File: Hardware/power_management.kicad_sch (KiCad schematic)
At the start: 37 parts, among them J2 Conn_01x03, SW27 SW_DPDT_x2, U2 BQ24040, U3 BQ51050BRHL, U4 AP22814BW5, U5 AP7333

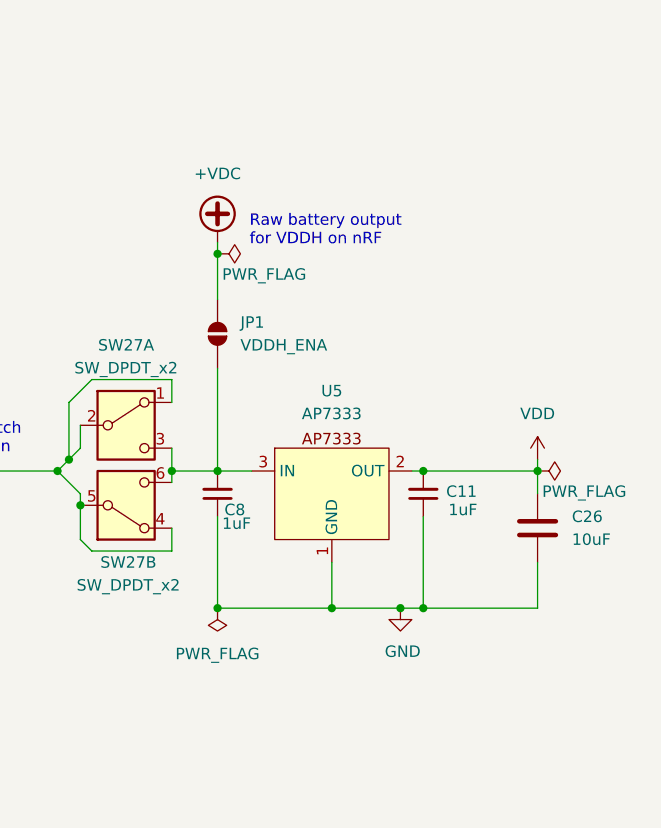
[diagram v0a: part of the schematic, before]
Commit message: Removed LDO (already one built into nrf)
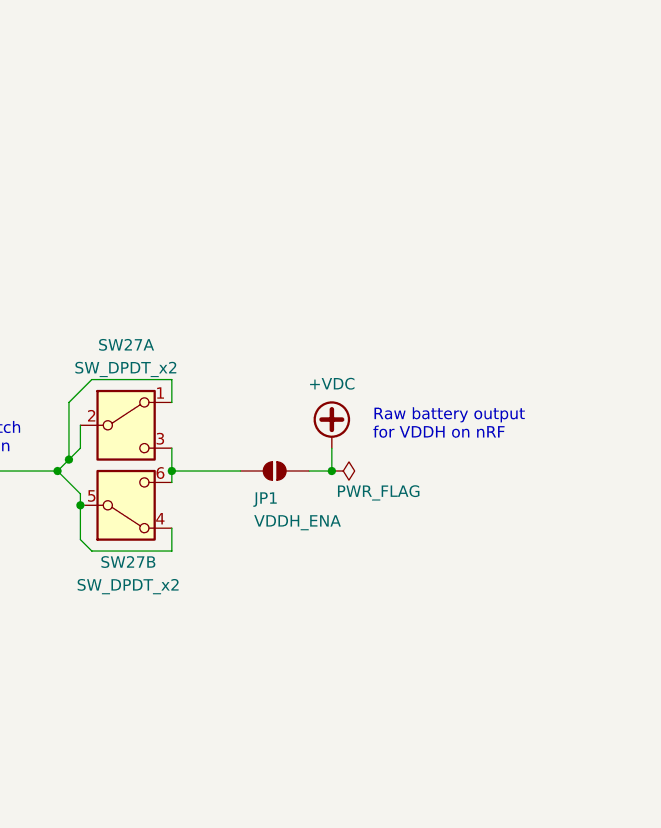
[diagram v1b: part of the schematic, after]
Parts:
- removed C11, C8: 1uF, Capacitor_SMD:C_0603_1608Metric, symbol Device:C_Small
- removed C26: 10uF, Capacitor_SMD:C_0603_1608Metric, symbol Device:C
- removed U5: AP7333, Package_TO_SOT_SMD:SOT-23, symbol Custom_sym:AP7333-33
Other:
- moved on the sheet: JP1

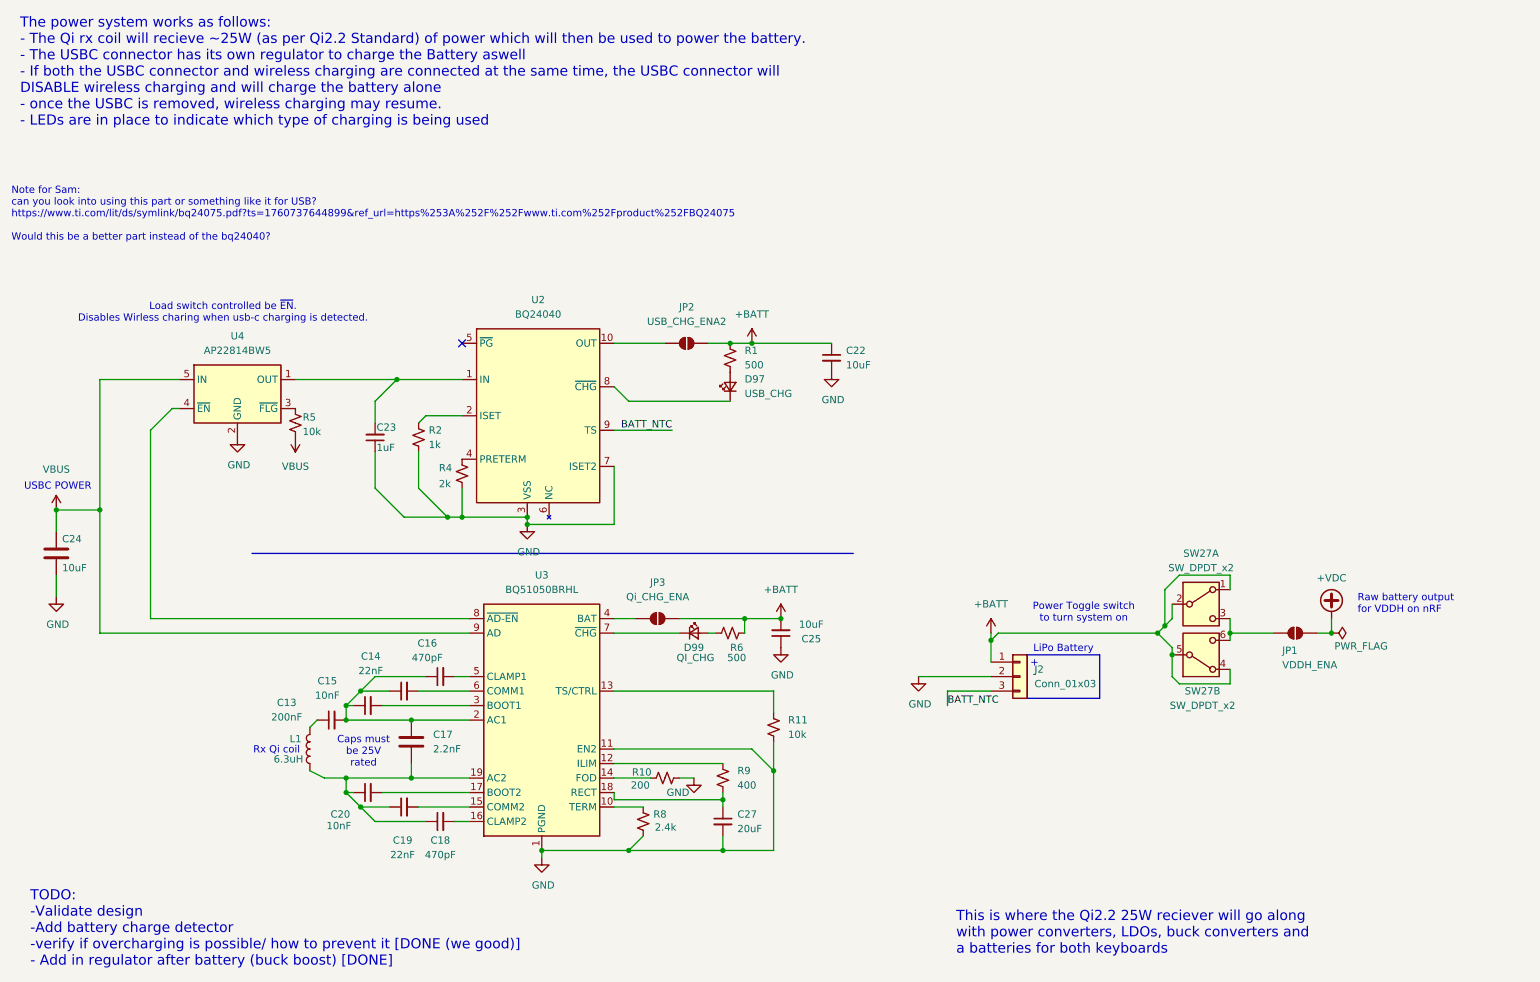
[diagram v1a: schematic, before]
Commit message: Update schematic for hornet_kb with new coordinates
Adjusted coordinates for arcs, text, junctions, no_connects, and wires in hornet_kb.kicad_sch to reflect a new layout or grid. This includes moving various elements to new positions, removing and adding connections, and updating wire paths for improved schematic organization and clarity.
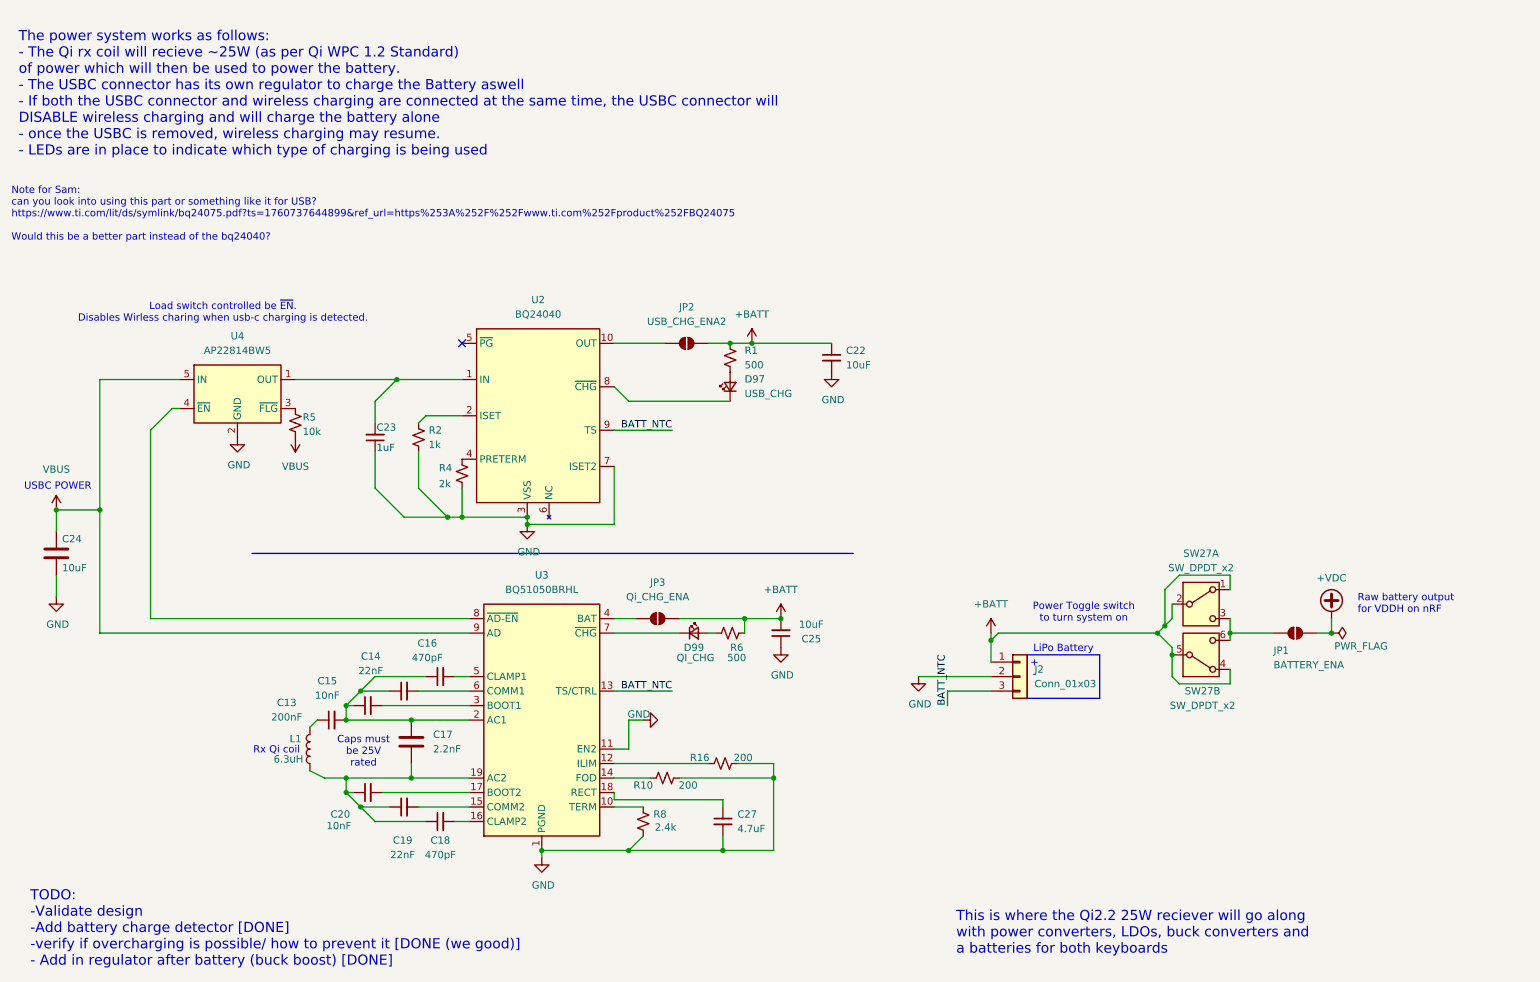
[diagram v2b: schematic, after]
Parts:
- removed R11: 10k, Resistor_SMD:R_0603_1608Metric, symbol Device:R_Small_US
- removed R9: 400, Resistor_SMD:R_0603_1608Metric, symbol Device:R_Small_US
- added R16: 200, Resistor_SMD:R_0603_1608Metric, symbol Device:R_Small_US
- C27: value 20uF -> 4.7uF
- JP1: value VDDH_ENA -> BATTERY_ENA
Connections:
- net BATT_NTC: now also U3.13 (TS/CTRL)
- net GND: now also R16.2
- net at U3.12 (ILIM): now also R16.1
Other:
- note added: "TODO: -Validate design -Add battery charge detector [DONE] -verify if overcharging is possible/ how to prevent it [DONE (we good)] - Add in regulator after battery (buck boost) [DONE]"
- note added: "The power system works as follows: - The Qi rx coil will recieve ~25W (as per Qi WPC 1.2 Standard) of power which will then be used to power the battery. - The USBC connector has its own regulator to charge the Battery aswell - If both the USBC connector and wireless charging are connected at the same time, the USBC connector will DISABLE wireless charging and will charge the battery alone - once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"
- note removed: "TODO: -Validate design -Add battery charge detector -verify if overcharging is possible/ how to prevent it [DONE (we good)] - Add in regulator after battery (buck boost) [DONE]"
- note removed: "The power system works as follows: - The Qi rx coil will recieve ~25W (as per Qi2.2 Standard) of power which will then be used to power the battery. - The USBC connector has its own regulator to charge the Battery aswell - If both the USBC connector and wireless charging are connected at the same time, the USBC connector will DISABLE wireless charging and will charge the battery alone - once the 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"

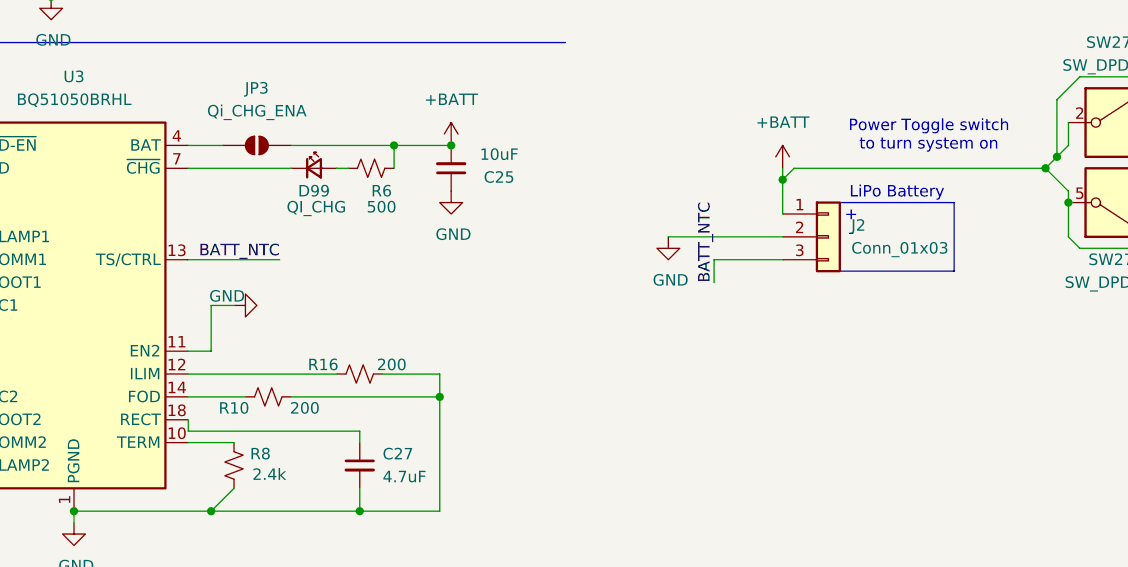
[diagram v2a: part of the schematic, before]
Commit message: Update schematic files and add image to hornet_kb
Adjusted text position in hornet_kb.kicad_sch, added a large embedded image, and updated key_matrix and power_management schematic files. These changes may improve documentation and visual references within the hardware schematics.
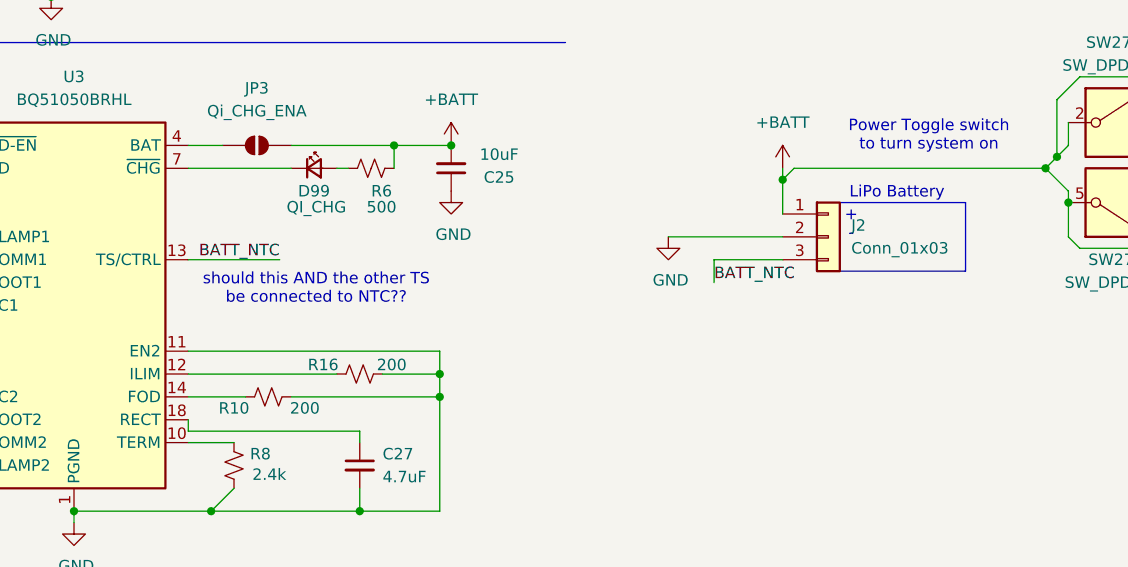
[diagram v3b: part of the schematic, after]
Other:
- note added: "should this AND the other TS be connected to NTC??"
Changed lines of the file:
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@@
 		(rev "1")
 	)
+	(text "should this AND the other TS\nbe connected to NTC??"
+		(exclude_from_sim no)
+		(at 133.604 134.112 0)
+		(effects
+			(font
+				(size 1.27 1.27)
+			)
+		)
+	)
 	(text "Rx Qi coil\n"
 		(exclude_from_sim no)
@@
 	)
 	(junction
+		(at 147.32 143.51)
+		(diameter 0)
+		(color 0 0 0 0)
+	)
+	(junction
 		(at 81.28 76.2)
 		(diameter 0)
@@
 	(polyline
 		(pts
-			(xy 191.77 132.08) (xy 204.47 132.08)
+			(xy 191.77 132.08) (xy 205.74 132.08)
 		)
 		(stroke
@@
 	(wire
 		(pts
-			(xy 147.32 143.51) (xy 147.32 146.05)
+			(xy 74.93 130.81) (xy 77.47 128.27)
 		)
 		(stroke
@@
 	(wire
 		(pts
-			(xy 74.93 130.81) (xy 77.47 128.27)
+			(xy 85.09 130.81) (xy 93.98 130.81)
 		)
 		(stroke
@@
 	(wire
 		(pts
-			(xy 85.09 130.81) (xy 93.98 130.81)
+			(xy 217.17 124.46) (xy 217.17 128.27)
 		)
 		(stroke
@@
 	(wire
 		(pts
-			(xy 217.17 124.46) (xy 217.17 128.27)
+			(xy 72.39 146.05) (xy 72.39 148.59)
 		)
 		(stroke
@@
 	(wire
 		(pts
-			(xy 72.39 146.05) (xy 72.39 148.59)
+			(xy 147.32 143.51) (xy 147.32 146.05)
 		)
 		(stroke
@@
 		)
 	)
-	(wire
-		(pts
-			(xy 121.92 135.89) (xy 124.46 135.89)
-		)
-		(stroke
-			(width 0)
-			(type default)
-		)
-	)
 	(polyline
 		(pts
@@
 	(wire
 		(pts
-			(xy 74.93 130.81) (xy 72.39 133.35)
+			(xy 147.32 140.97) (xy 147.32 143.51)
 		)
 		(stroke
@@
 	(wire
 		(pts
-			(xy 121.92 135.89) (xy 121.92 140.97)
+			(xy 74.93 130.81) (xy 72.39 133.35)
 		)
 		(stroke
@@
 	(polyline
 		(pts
-			(xy 204.47 124.46) (xy 204.47 132.08)
+			(xy 205.74 124.46) (xy 205.74 132.08)
 		)
 		(stroke
@@
 	(wire
 		(pts
-			(xy 119.38 140.97) (xy 121.92 140.97)
+			(xy 119.38 140.97) (xy 147.32 140.97)
 		)
 		(stroke
@@
 	(polyline
 		(pts
-			(xy 191.77 124.46) (xy 204.47 124.46)
+			(xy 191.77 124.46) (xy 205.74 124.46)
 		)
 		(stroke
@@
 	)
 	(label "BATT_NTC"
-		(at 177.8 133.35 90)
+		(at 177.8 133.35 0)
 		(effects
 			(font
@@
 					(unit 1)
 				)
-			)
-		)
-	)
-	(symbol
-		(lib_id "power:GND")
-		(at 124.46 135.89 90)
-		(mirror x)
-		(unit 1)
-		(exclude_from_sim no)
-		(in_bom yes)
-		(on_board yes)
-		(dnp no)
-		(property "Reference" "#PWR027"
-			(at 130.81 135.89 0)
-			(effects
-				(font
-					(size 1.27 1.27)
-				)
-				(hide yes)
-			)
-		)
-		(property "Value" "GND"
-			(at 123.698 134.874 90)
-			(effects
-				(font
-					(size 1.27 1.27)
-				)
-			)
-		)
-		(property "Footprint" ""
-			(at 124.46 135.89 0)
-			(effects
-				(font
-					(size 1.27 1.27)
-				)
-				(hide yes)
-			)
-		)
-		(property "Datasheet" ""
-			(at 124.46 135.89 0)
-			(effects
-				(font
-					(size 1.27 1.27)
-				)
-				(hide yes)
-			)
-		)
-		(property "Description" "Power symbol creates a global label with name \"GND\" , ground"
-			(at 124.46 135.89 0)
-			(effects
-				(font
-					(size 1.27 1.27)
-				)
-				(hide yes)
-			)
-		)
-		(pin "1"
-		)
-		(instances
-			(project "hornet_kb"
-				(path "/c35084ab-104c-4a4c-9388-a839989b8e3d/20e65fb9-037d-41f9-856c-d800ba40b4b1"
-					(reference "#PWR027")
-					(unit 1)
-				)
